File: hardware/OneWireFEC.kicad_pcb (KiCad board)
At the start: 2 copper layers, 24 x 27.9 mm, 23 parts, among them J1 105444-0001, J2 B2B-XH-A, U1 PIC16F1454, U2 DS2482S, U3 AP22652

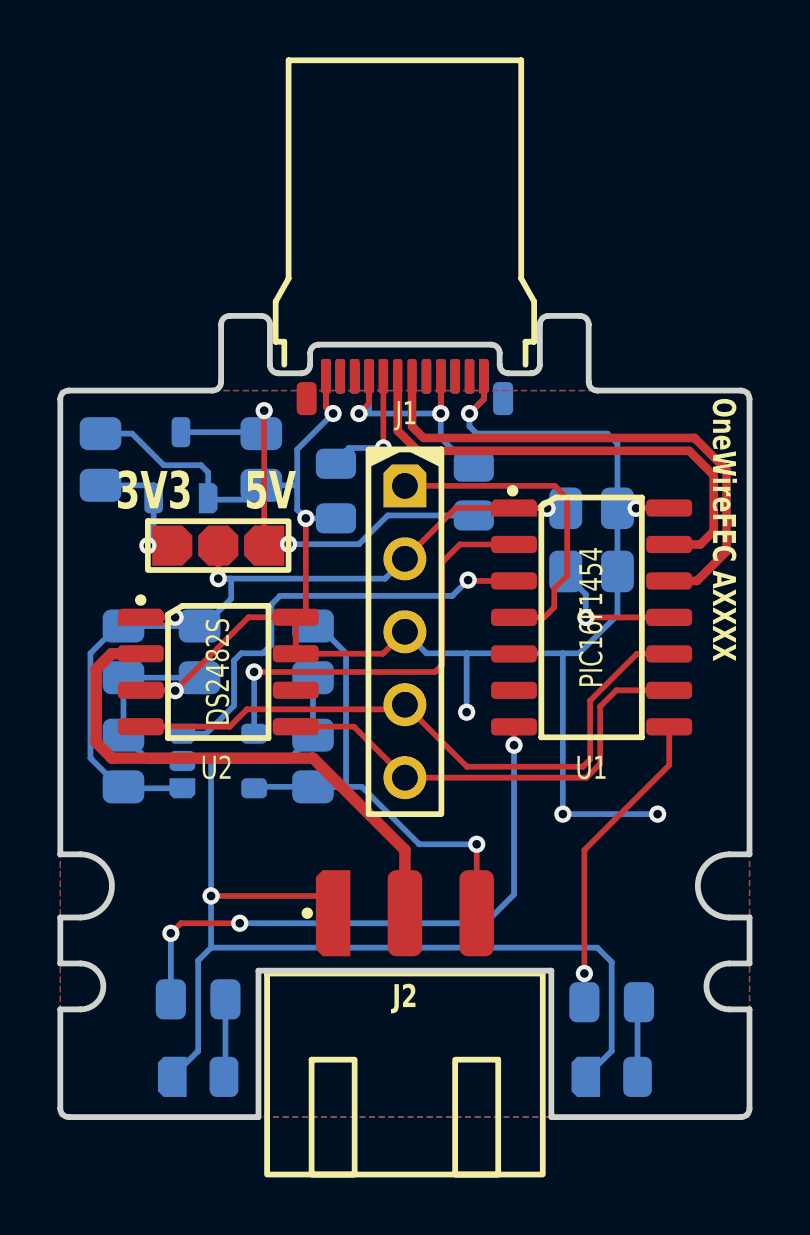
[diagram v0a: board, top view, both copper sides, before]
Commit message: Added pull-up resistors for I2C and added Vusb3V3 jumper
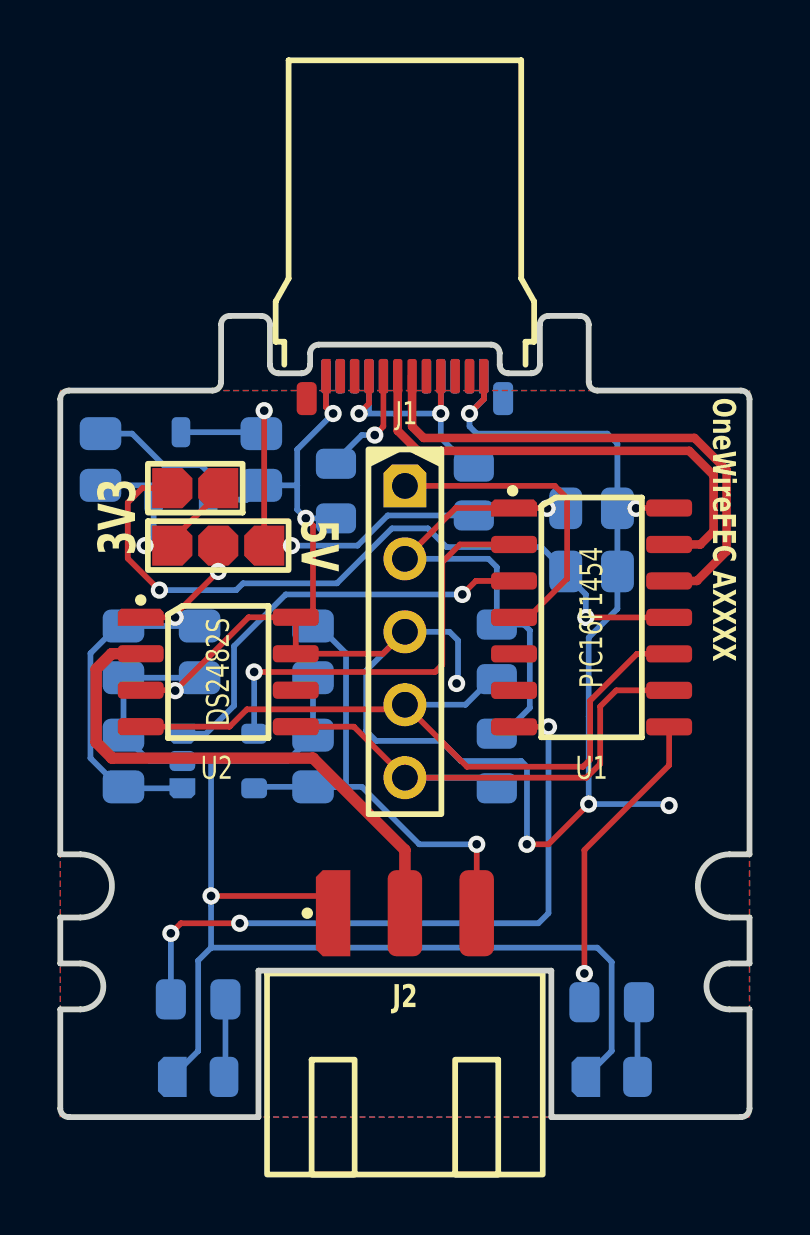
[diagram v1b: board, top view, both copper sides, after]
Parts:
- added JP2: Jumper, Medo64:JP (0805), F.Cu at (24.7, 26.0)
- added R3: 3K3, Medo64:R (0805), B.Cu at (35.2, 31.7)
- added R4: 3K3, Medo64:R (0805), B.Cu at (35.2, 35.5)
- renumbered R3 to R5
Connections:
- net V33 renamed 3V3_USB
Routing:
- net 3V3_USB: track 4.55 -> 25.5 mm, vias 1 -> 2
- net GND: track 116.6 -> 126.5 mm, vias 9 -> 10
- net VDD: track 29.7 -> 33.7 mm
- net SCL: track 22.2 -> 25.8 mm
- net SDA: track 16.2 -> 19.5 mm
- net 3V3: track 4.75 -> 7.54 mm
- net LED_A: track 20.6 -> 23.4 mm
- net POWER_EN: track 15.5 -> 15.0 mm

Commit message: Fixed a few typos
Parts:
- U3: value AP22652 -> MIC2091
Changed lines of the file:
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@@
         (effects (font (size 0.8 0.6) (thickness 0.15)) (justify mirror))
     )
-    (fp_text value "AP22652" (at 0 -2.4 -360) (layer "B.SilkS") hide
+    (fp_text value "MIC2091" (at 0 -2.4 -360) (layer "B.SilkS") hide
         (effects (font (size 0.8 0.6) (thickness 0.15)) (justify mirror))
     )

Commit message: Added output labels
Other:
- board text added: "DQ"
- board text added: "GND"
- board text added: "VDD"
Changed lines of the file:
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@@
   (gr_circle locked (center 20.7 39.85) (end 23.15 39.85)
     (stroke (width 0.01) (type solid)) (fill none) (layer "Margin"))
+  (gr_text "VDD" (at 34.55 39.1) (layer "F.SilkS" knockout)
+    (effects (font (size 1.3 0.9) (thickness 0.15) bold) (justify bottom))
+  )
   (gr_text "5V" (at 29 28 270) (layer "F.SilkS" knockout)
     (effects (font (size 1.3 0.9) (thickness 0.15) bold))
+  )
+  (gr_text "DQ" (at 31.95 39) (layer "F.SilkS" knockout)
+    (effects (font (size 1.3 0.9) (thickness 0.15) bold) (justify bottom))
   )
   (gr_text "OneWireFEC AXXXX" (at 43.1 22.85 270) (layer "F.SilkS")
@@
     (effects (font (size 1.3 0.9) (thickness 0.15) bold))
   )
+  (gr_text "GND" (at 29.4 39.1) (layer "F.SilkS" knockout)
+    (effects (font (size 1.3 0.9) (thickness 0.15) bold) (justify bottom))
+  )
   (segment (start 31.25 23.85) (end 30.95 24.15) (width 0.2) (layer "F.Cu") (net 1))

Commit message: Refactoring
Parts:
- U1: footprint Medo64:U Micro PIC16F1454 (SOIC-14) -> Medo64:U Micro [PIC16F1454] (SOIC-14)
- U2: footprint Medo64:U Transciever 1Wire DS2482S (SOIC-8) -> Medo64:U Transceiver 1Wire [DS2482S-100+] (SOIC-8)
- U3: footprint Medo64:U LoadSwitch MIC2091 (SOT23-5) -> Medo64:U LoadSwitch 100mA [MIC2091-1] (SOT23-5)
- VR1: footprint Medo64:VR Linear MCP1700 (SOT23-3) -> Medo64:VR Linear 3.3V 250mA [MCP1700] (SOT-23)
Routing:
- net VDD: track 33.7 -> 39.8 mm
- net SDA: track 19.5 -> 19.0 mm
- net ICSP_VPP: track 11.0 -> 10.5 mm
